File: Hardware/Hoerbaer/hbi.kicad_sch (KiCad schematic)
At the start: 50 parts, among them J10 LEDS, J11 LEDS, J6 BUTTONS, J7 BUTTONS, J8 BUTTONS, J9 LEDS, U2 PCF8574TS, U3 PCF8574TS, U4 PCF8574TS, U5 TLC59108xPW, U6 TLC59108xPW, U7 TLC59108xPW

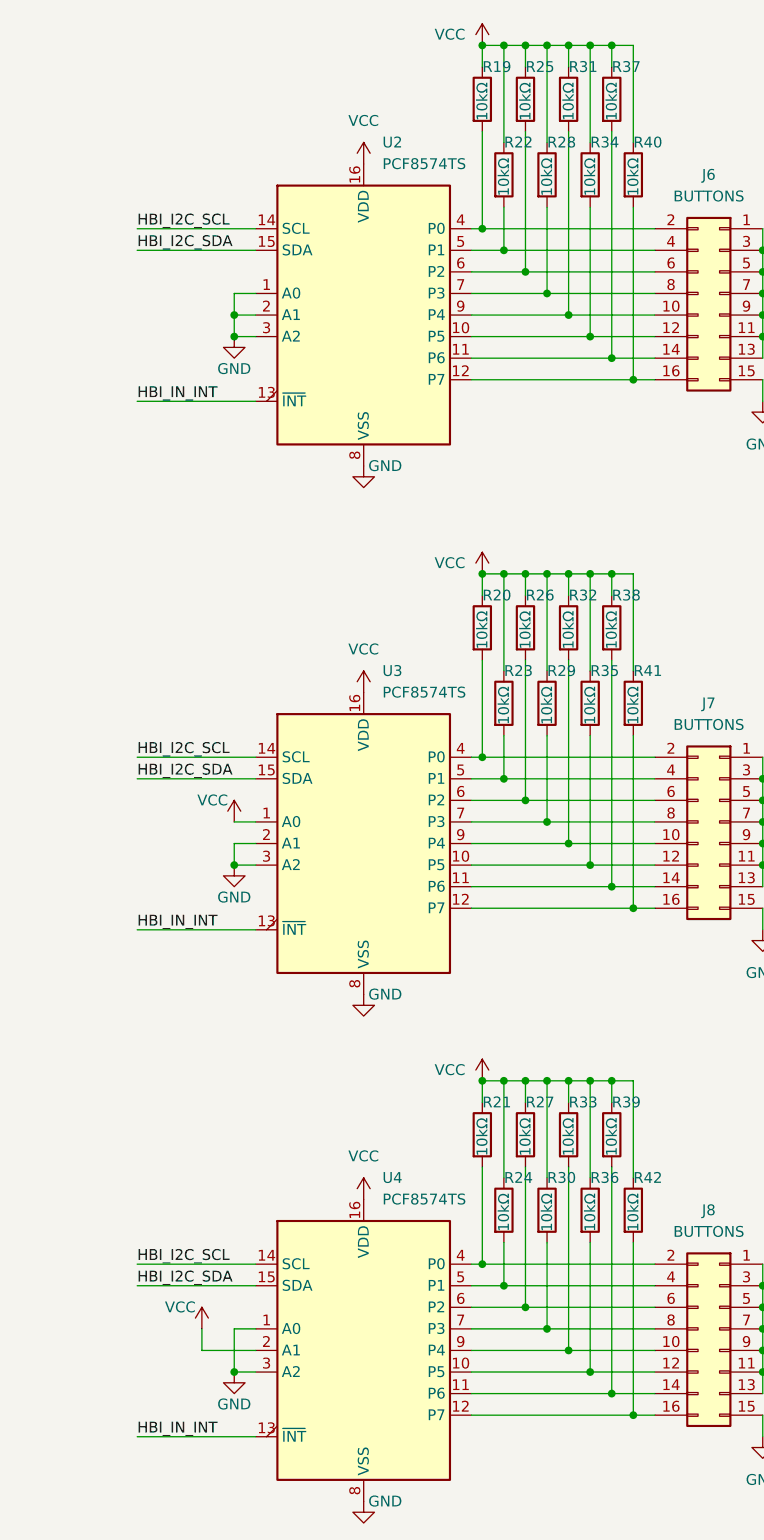
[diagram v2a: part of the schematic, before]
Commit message: More numbers, changed HBI input package, i2c addresses, layout.
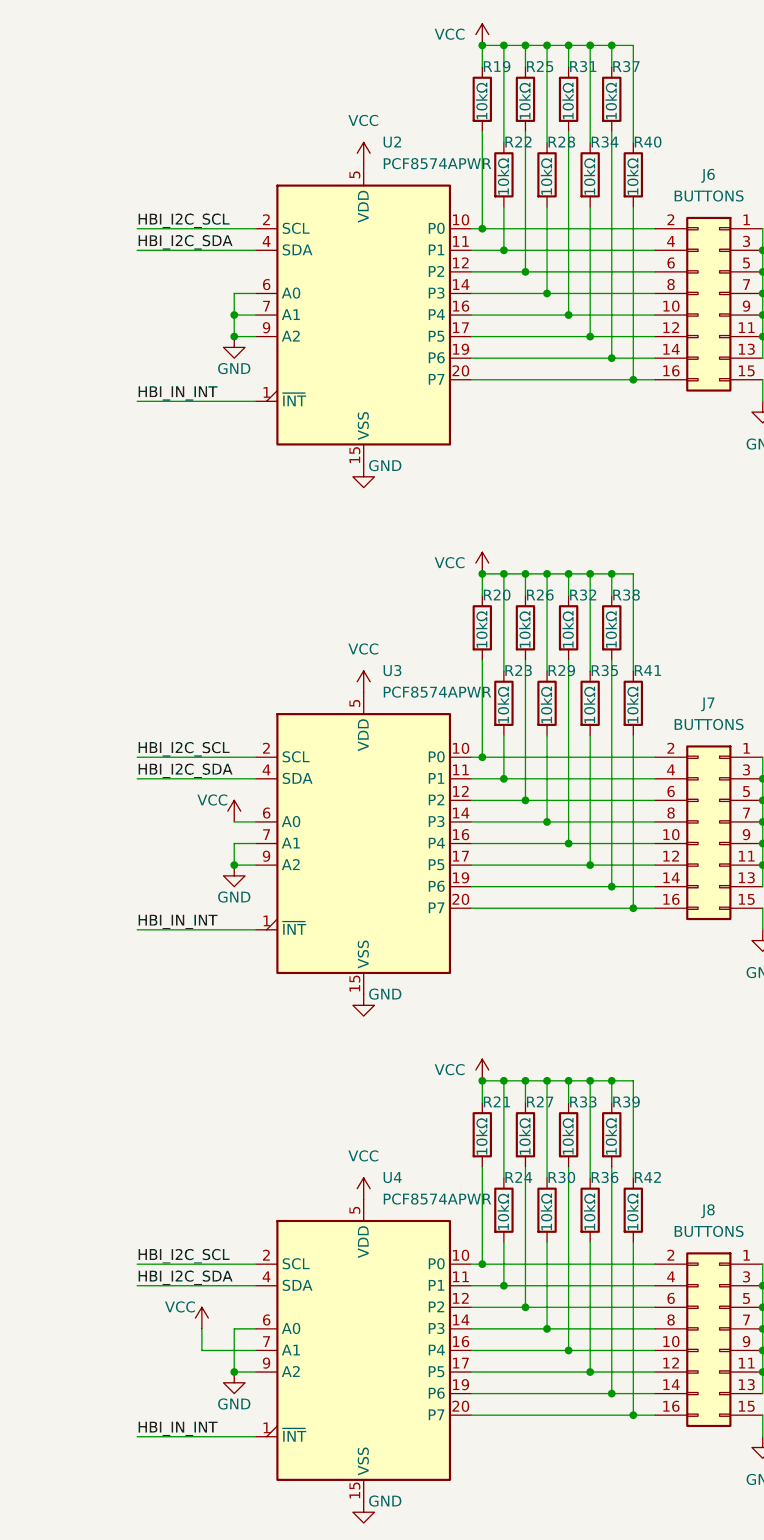
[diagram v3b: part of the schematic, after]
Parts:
- U2, U3, U4: value PCF8574TS -> PCF8574APWR; footprint Package_SO:SOIC-16W_7.5x10.3mm_P1.27mm -> Package_SO:SSOP-20_4.4x6.5mm_P0.65mm; symbol Interface_Expansion:PCF8574A -> Interface_Expansion:PCF8574ATS; JLCPCB C2987289 -> C94361; MPN PCF8574AT/TR -> PCF8574APWR
- U5: JLCPCB (none) -> C130031; MPN (none) -> TLC59108IPWR
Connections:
- net GND: now also U2.15 (VSS), U2.6 (A0), U2.7 (A1), U2.9 (A2), U3.15 (VSS), U3.7 (A1), U3.9 (A2), U4.15 (VSS), U4.6 (A0), U4.9 (A2); no longer U2.1 (A0), U2.2 (A1), U2.3 (A2), U2.8 (VSS), U3.2 (A1), U3.3 (A2), U3.8 (VSS), U4.1 (A0), U4.3 (A2), U4.8 (VSS)
- net HBI_I2C_SCL: now also U2.2 (SCL), U3.2 (SCL), U4.2 (SCL); no longer U2.14 (SCL), U3.14 (SCL), U4.14 (SCL)
- net HBI_I2C_SDA: now also U2.4 (SDA), U3.4 (SDA), U4.4 (SDA); no longer U2.15 (SDA), U3.15 (SDA), U4.15 (SDA)
- net HBI_IN_INT: now also U2.1 (~{INT}), U3.1 (~{INT}), U4.1 (~{INT}); no longer U2.13 (~{INT}), U3.13 (~{INT}), U4.13 (~{INT})
- net VCC: now also U2.5 (VDD), U3.5 (VDD), U3.6 (A0), U4.5 (VDD), U4.7 (A1); no longer U2.16 (VDD), U3.1 (A0), U3.16 (VDD), U4.16 (VDD), U4.2 (A1)
- net at J8.4 (Pin_4), R24.2: now also U4.11 (P1); no longer U4.5 (P1)
- net at J6.2 (Pin_2), R19.2: now also U2.10 (P0); no longer U2.4 (P0)
- net at J7.8 (Pin_8), R29.2: now also U3.14 (P3); no longer U3.7 (P3)
- net at J8.12 (Pin_12), R36.2: now also U4.17 (P5); no longer U4.10 (P5)
- net at J8.14 (Pin_14), R39.2: now also U4.19 (P6); no longer U4.11 (P6)
- net at J8.16 (Pin_16), R42.2: now also U4.20 (P7); no longer U4.12 (P7)
- net at J8.2 (Pin_2), R21.2: now also U4.10 (P0); no longer U4.4 (P0)
- net at J8.6 (Pin_6), R27.2: now also U4.12 (P2); no longer U4.6 (P2)
- net at J8.8 (Pin_8), R30.2: now also U4.14 (P3); no longer U4.7 (P3)
- net at J8.10 (Pin_10), R33.2: now also U4.16 (P4); no longer U4.9 (P4)
- net at J7.12 (Pin_12), R35.2: now also U3.17 (P5); no longer U3.10 (P5)
- net at J7.14 (Pin_14), R38.2: now also U3.19 (P6); no longer U3.11 (P6)
- net at J7.16 (Pin_16), R41.2: now also U3.20 (P7); no longer U3.12 (P7)
- net at J7.2 (Pin_2), R20.2: now also U3.10 (P0); no longer U3.4 (P0)
- net at J7.4 (Pin_4), R23.2: now also U3.11 (P1); no longer U3.5 (P1)
- net at J7.6 (Pin_6), R26.2: now also U3.12 (P2); no longer U3.6 (P2)
- net at J7.10 (Pin_10), R32.2: now also U3.16 (P4); no longer U3.9 (P4)
- net at J6.6 (Pin_6), R25.2: now also U2.12 (P2); no longer U2.6 (P2)
- net at J6.12 (Pin_12), R34.2: now also U2.17 (P5); no longer U2.10 (P5)
- net at J6.10 (Pin_10), R31.2: now also U2.16 (P4); no longer U2.9 (P4)
- net at J6.14 (Pin_14), R37.2: now also U2.19 (P6); no longer U2.11 (P6)
- net at J6.16 (Pin_16), R40.2: now also U2.20 (P7); no longer U2.12 (P7)
- net at J6.4 (Pin_4), R22.2: now also U2.11 (P1); no longer U2.5 (P1)
- net at J6.8 (Pin_8), R28.2: now also U2.14 (P3); no longer U2.7 (P3)

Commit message: Layout drc error free
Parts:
- removed J10, J11, J9: LEDS, Connector_PinHeader_2.54mm:PinHeader_2x08_P2.54mm_Vertical, symbol Connector_Generic:Conn_02x08_Odd_Even
- removed J7, J8: BUTTONS, Connector_PinHeader_2.54mm:PinHeader_2x08_P2.54mm_Vertical, symbol Connector_Generic:Conn_02x08_Odd_Even
- added C65: 10µF, Capacitor_SMD:C_0805_2012Metric, symbol Device:C
- added J7: PAW_B, Connector_PinHeader_2.54mm:PinHeader_2x12_P2.54mm_Vertical, symbol Connector_Generic:Conn_02x12_Odd_Even
- added J8: PAW_C, Connector_PinHeader_2.54mm:PinHeader_2x12_P2.54mm_Vertical, symbol Connector_Generic:Conn_02x12_Odd_Even
- added J9: PAW_D, Connector_PinHeader_2.54mm:PinHeader_2x12_P2.54mm_Vertical, symbol Connector_Generic:Conn_02x12_Odd_Even
- J6: value BUTTONS -> PAW_A; footprint Connector_PinHeader_2.54mm:PinHeader_2x08_P2.54mm_Vertical -> Connector_PinHeader_2.54mm:PinHeader_2x12_P2.54mm_Vertical; symbol Connector_Generic:Conn_02x08_Odd_Even -> Connector_Generic:Conn_02x12_Odd_Even
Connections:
- net +12V: now also J6.12 (Pin_12), J6.16 (Pin_16), J6.20 (Pin_20), J6.24 (Pin_24), J6.4 (Pin_4), J6.8 (Pin_8), C65.1, J7.12 (Pin_12), J7.16 (Pin_16), J7.20 (Pin_20), J7.24 (Pin_24), J7.4 (Pin_4), J7.8 (Pin_8), J8.12 (Pin_12), J8.16 (Pin_16), J8.20 (Pin_20), J8.24 (Pin_24), J8.4 (Pin_4), J8.8 (Pin_8), J9.12 (Pin_12), J9.16 (Pin_16), J9.20 (Pin_20), J9.24 (Pin_24), J9.4 (Pin_4), J9.8 (Pin_8)
- net GND: now also J6.10 (Pin_10), J6.14 (Pin_14), J6.18 (Pin_18), J6.2 (Pin_2), J6.22 (Pin_22), J6.6 (Pin_6), C65.2, J7.10 (Pin_10), J7.14 (Pin_14), J7.18 (Pin_18), J7.2 (Pin_2), J7.22 (Pin_22), J7.6 (Pin_6), J8.10 (Pin_10), J8.14 (Pin_14), J8.18 (Pin_18), J8.2 (Pin_2), J8.22 (Pin_22), J8.6 (Pin_6), J9.10 (Pin_10), J9.14 (Pin_14), J9.18 (Pin_18), J9.2 (Pin_2), J9.22 (Pin_22), J9.6 (Pin_6); no longer J6.15 (Pin_15)
- net PAW_C_B6: now reaches R24.2, U4.11 (P1)
- net PAW_C_B6: now also J8.21 (Pin_21)
- net PAW_A_B1: now reaches R19.2, U2.10 (P0)
- net PAW_A_B1: now also J6.1 (Pin_1); no longer J6.2 (Pin_2)
- net PAW_B_B6: now reaches R29.2, U3.14 (P3)
- net PAW_B_B6: now also J7.21 (Pin_21)
- net PAW_C_B5: now reaches R21.2, U4.10 (P0)
- net PAW_C_B5: now also J8.17 (Pin_17)
- net PAW_D_B1: now reaches R27.2, U4.12 (P2)
- net PAW_D_B1: now also J9.1 (Pin_1)
- net PAW_D_B2: now reaches R30.2, U4.14 (P3)
- net PAW_D_B2: now also J9.5 (Pin_5)
- net PAW_D_B3: now reaches R33.2, U4.16 (P4)
- net PAW_D_B3: now also J9.9 (Pin_9)
- net PAW_D_B4: now reaches R36.2, U4.17 (P5)
- net PAW_D_B4: now also J9.13 (Pin_13)
- net PAW_D_B5: now reaches R39.2, U4.19 (P6)
- net PAW_D_B5: now also J9.17 (Pin_17)
- net PAW_D_B6: now reaches R42.2, U4.20 (P7)
- net PAW_D_B6: now also J9.21 (Pin_21)
- net PAW_B_B3: now reaches R20.2, U3.10 (P0)
- net PAW_B_B3: now also J7.9 (Pin_9)
- net PAW_B_B4: now reaches R23.2, U3.11 (P1)
- net PAW_B_B4: now also J7.13 (Pin_13)
- net PAW_B_B5: now reaches R26.2, U3.12 (P2)
- net PAW_B_B5: now also J7.17 (Pin_17)
- net PAW_C_B1: now reaches R32.2, U3.16 (P4)
- net PAW_C_B1: now also J8.1 (Pin_1)
- net PAW_C_B2: now reaches R35.2, U3.17 (P5)
- net PAW_C_B2: now also J8.5 (Pin_5)
- net PAW_C_B3: now reaches R38.2, U3.19 (P6)
- net PAW_C_B3: now also J8.9 (Pin_9)
- net PAW_C_B4: now reaches R41.2, U3.20 (P7)
- net PAW_C_B4: now also J8.13 (Pin_13)
- net PAW_A_B3: now reaches R25.2, U2.12 (P2)
- net PAW_A_B3: now also J6.9 (Pin_9); no longer J6.6 (Pin_6)
- net PAW_D_D2: now reaches U7.10 (~{OUT3})
- net PAW_D_D2: now also J9.7 (Pin_7)
- net PAW_D_D3: now reaches U7.11 (~{OUT4})
- net PAW_D_D3: now also J9.11 (Pin_11)
- net PAW_D_D4: now reaches U7.12 (~{OUT5})
- net PAW_D_D4: now also J9.15 (Pin_15)
- net PAW_D_D5: now reaches U7.14 (~{OUT6})
- net PAW_D_D5: now also J9.19 (Pin_19)
- net PAW_D_D6: now reaches U7.15 (~{OUT7})
- net PAW_D_D6: now also J9.23 (Pin_23)
- net PAW_C_D5: now reaches U7.6 (~{OUT0})
- net PAW_C_D5: now also J8.19 (Pin_19)
- net PAW_C_D6: now reaches U7.7 (~{OUT1})
- net PAW_C_D6: now also J8.23 (Pin_23)
- net PAW_D_D1: now reaches U7.9 (~{OUT2})
- net PAW_D_D1: now also J9.3 (Pin_3)
- net PAW_A_B6: now reaches R34.2, U2.17 (P5)
- net PAW_A_B6: now also J6.21 (Pin_21); no longer J6.12 (Pin_12)
- net PAW_A_B5: now reaches R31.2, U2.16 (P4)
- net PAW_A_B5: now also J6.17 (Pin_17); no longer J6.10 (Pin_10)
- net PAW_B_B1: now reaches R37.2, U2.19 (P6)
- net PAW_B_B1: now also J7.1 (Pin_1); no longer J6.14 (Pin_14)
- net PAW_B_B2: now reaches R40.2, U2.20 (P7)
- net PAW_B_B2: now also J7.5 (Pin_5); no longer J6.16 (Pin_16)
- net PAW_A_B2: now reaches R22.2, U2.11 (P1)
- net PAW_A_B2: now also J6.5 (Pin_5); no longer J6.4 (Pin_4)
- net PAW_A_B4: now reaches R28.2, U2.14 (P3)
- net PAW_A_B4: now also J6.13 (Pin_13); no longer J6.8 (Pin_8)
- net PAW_A_D4: now reaches U5.10 (~{OUT3})
- net PAW_A_D4: now also J6.15 (Pin_15)
- net PAW_A_D5: now reaches U5.11 (~{OUT4})
- net PAW_A_D5: now also J6.19 (Pin_19)
- net PAW_A_D6: now reaches U5.12 (~{OUT5})
- net PAW_A_D6: now also J6.23 (Pin_23)
- net PAW_B_D1: now reaches U5.14 (~{OUT6})
- net PAW_B_D1: now also J7.3 (Pin_3)
- net PAW_B_D2: now reaches U5.15 (~{OUT7})
- net PAW_B_D2: now also J7.7 (Pin_7)
- net PAW_A_D1: now reaches U5.6 (~{OUT0})
- net PAW_A_D1: now also J6.3 (Pin_3)
- net PAW_A_D2: now reaches U5.7 (~{OUT1})
- net PAW_A_D2: now also J6.7 (Pin_7)
- net PAW_A_D3: now reaches U5.9 (~{OUT2})
- net PAW_A_D3: now also J6.11 (Pin_11)
- net PAW_B_D6: now reaches U6.10 (~{OUT3})
- net PAW_B_D6: now also J7.23 (Pin_23)
- net PAW_C_D1: now reaches U6.11 (~{OUT4})
- net PAW_C_D1: now also J8.3 (Pin_3)
- net PAW_C_D2: now reaches U6.12 (~{OUT5})
- net PAW_C_D2: now also J8.7 (Pin_7)
- net PAW_C_D3: now reaches U6.14 (~{OUT6})
- net PAW_C_D3: now also J8.11 (Pin_11)
- net PAW_C_D4: now reaches U6.15 (~{OUT7})
- net PAW_C_D4: now also J8.15 (Pin_15)
- net PAW_B_D3: now reaches U6.6 (~{OUT0})
- net PAW_B_D3: now also J7.11 (Pin_11)
- net PAW_B_D4: now reaches U6.7 (~{OUT1})
- net PAW_B_D4: now also J7.15 (Pin_15)
- net PAW_B_D5: now reaches U6.9 (~{OUT2})
- net PAW_B_D5: now also J7.19 (Pin_19)
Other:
- note removed: "R_{EXT} 2kΩ => LED current: 1mA"
- moved on the sheet: C10, C11, C22, C23, C24, C6, C7, C8, C9, R19, R20, R21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

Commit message: Order numbers
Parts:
- C10, C11, C6, C7, C8, C9: JLCPCB (none) -> C458949; MPN (none) -> MT15B104K160CT
- U6, U7: JLCPCB (none) -> C130031; MPN (none) -> TLC59108IPWR
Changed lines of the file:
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@@
+      (effects (font (size 1.27 1.27)) hide)
+    )
+    (property "JLCPCB" "C458949" (at 99.06 110.49 0)
+      (effects (font (size 1.27 1.27)) hide)
+    )
+    (property "MPN" "MT15B104K160CT" (at 99.06 110.49 0)
       (effects (font (size 1.27 1.27)) hide)
     )
@@
       (effects (font (size 1.27 1.27)) hide)
     )
+    (property "JLCPCB" "C130031" (at 242.57 139.7 0)
+      (effects (font (size 1.27 1.27)) hide)
+    )
+    (property "MPN" "TLC59108IPWR" (at 242.57 139.7 0)
+      (effects (font (size 1.27 1.27)) hide)
+    )
     (pin "1")
     (pin "10")
@@
       (effects (font (size 1.27 1.27)) hide)
     )
+    (property "JLCPCB" "C458949" (at 214.63 46.99 0)
+      (effects (font (size 1.27 1.27)) hide)
+    )
+    (property "MPN" "MT15B104K160CT" (at 214.63 46.99 0)
+      (effects (font (size 1.27 1.27)) hide)
+    )
     (pin "1")
     (pin "2")
@@
       (effects (font (size 1.27 1.27)) hide)
     )
+    (property "JLCPCB" "C458949" (at 99.06 48.26 0)
+      (effects (font (size 1.27 1.27)) hide)
+    )
+    (property "MPN" "MT15B104K160CT" (at 99.06 48.26 0)
+      (effects (font (size 1.27 1.27)) hide)
+    )
     (pin "1")
     (pin "2")
@@
       (effects (font (size 1.27 1.27)) hide)
     )
+    (property "JLCPCB" "C458949" (at 214.63 151.13 0)
+      (effects (font (size 1.27 1.27)) hide)
+    )
+    (property "MPN" "MT15B104K160CT" (at 214.63 151.13 0)
+      (effects (font (size 1.27 1.27)) hide)
+    )
     (pin "1")
     (pin "2")
@@
     )
     (property "Datasheet" "~" (at 99.06 170.18 0)
+      (effects (font (size 1.27 1.27)) hide)
+    )
+    (property "JLCPCB" "C458949" (at 99.06 170.18 0)
+      (effects (font (size 1.27 1.27)) hide)
+    )
+    (property "MPN" "MT15B104K160CT" (at 99.06 170.18 0)
       (effects (font (size 1.27 1.27)) hide)
     )
@@
       (effects (font (size 1.27 1.27)) hide)
     )
+    (property "JLCPCB" "C130031" (at 242.57 90.17 0)
+      (effects (font (size 1.27 1.27)) hide)
+    )
+    (property "MPN" "TLC59108IPWR" (at 242.57 90.17 0)
+      (effects (font (size 1.27 1.27)) hide)
+    )
     (pin "1")
     (pin "10")
@@
       (effects (font (size 1.27 1.27)) hide)
     )
+    (property "JLCPCB" "C458949" (at 214.63 101.6 0)
+      (effects (font (size 1.27 1.27)) hide)
+    )
+    (property "MPN" "MT15B104K160CT" (at 214.63 101.6 0)
+      (effects (font (size 1.27 1.27)) hide)
+    )

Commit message: Renamed JLCPCB attribute to LCSC (plugin search list)
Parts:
- C10, C11, C6, C7, C8, C9: JLCPCB C458949 -> (none); LCSC (none) -> C458949
- C22, C23, C24, C65: JLCPCB C6119932 -> (none); LCSC (none) -> C6119932
- U2, U3, U4: JLCPCB C94361 -> (none); LCSC (none) -> C94361
- U5, U6, U7: JLCPCB C130031 -> (none); LCSC (none) -> C130031
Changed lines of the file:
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@@
       (effects (font (size 1.27 1.27)) hide)
     )
-    (property "JLCPCB" "C458949" (at 99.06 110.49 0)
+    (property "LCSC" "C458949" (at 99.06 110.49 0)
       (effects (font (size 1.27 1.27)) hide)
     )
@@
       (effects (font (size 1.27 1.27)) hide)
     )
-    (property "JLCPCB" "C94361" (at 130.81 172.72 0)
+    (property "LCSC" "C94361" (at 130.81 172.72 0)
       (effects (font (size 1.27 1.27)) hide)
     )
@@
       (effects (font (size 1.27 1.27)) hide)
     )
-    (property "JLCPCB" "C94361" (at 130.81 113.03 0)
+    (property "LCSC" "C94361" (at 130.81 113.03 0)
       (effects (font (size 1.27 1.27)) hide)
     )
@@
       (effects (font (size 1.27 1.27)) hide)
     )
-    (property "JLCPCB" "C130031" (at 242.57 139.7 0)
+    (property "LCSC" "C130031" (at 242.57 139.7 0)
       (effects (font (size 1.27 1.27)) hide)
     )
@@
       (effects (font (size 1.27 1.27)) hide)
     )
-    (property "JLCPCB" "C6119932" (at 64.77 64.77 0)
+    (property "LCSC" "C6119932" (at 64.77 64.77 0)
       (effects (font (size 1.27 1.27)) hide)
     )
@@
       (effects (font (size 1.27 1.27)) hide)
     )
-    (property "JLCPCB" "C130031" (at 242.57 39.37 0)
+    (property "LCSC" "C130031" (at 242.57 39.37 0)
       (effects (font (size 1.27 1.27)) hide)
     )
@@
       (effects (font (size 1.27 1.27)) hide)
     )
-    (property "JLCPCB" "C458949" (at 214.63 46.99 0)
+    (property "LCSC" "C458949" (at 214.63 46.99 0)
       (effects (font (size 1.27 1.27)) hide)
     )
@@
       (effects (font (size 1.27 1.27)) hide)
     )
-    (property "JLCPCB" "C6119932" (at 77.47 64.77 0)
+    (property "LCSC" "C6119932" (at 77.47 64.77 0)
       (effects (font (size 1.27 1.27)) hide)
     )
@@
       (effects (font (size 1.27 1.27)) hide)
     )
-    (property "JLCPCB" "C458949" (at 99.06 48.26 0)
+    (property "LCSC" "C458949" (at 99.06 48.26 0)
       (effects (font (size 1.27 1.27)) hide)
     )
@@
       (effects (font (size 1.27 1.27)) hide)
     )
-    (property "JLCPCB" "C458949" (at 214.63 151.13 0)
+    (property "LCSC" "C458949" (at 214.63 151.13 0)
       (effects (font (size 1.27 1.27)) hide)
     )
@@
       (effects (font (size 1.27 1.27)) hide)
     )
-    (property "JLCPCB" "C458949" (at 99.06 170.18 0)
+    (property "LCSC" "C458949" (at 99.06 170.18 0)
       (effects (font (size 1.27 1.27)) hide)
     )
@@
       (effects (font (size 1.27 1.27)) hide)
     )
-    (property "JLCPCB" "C130031" (at 242.57 90.17 0)
+    (property "LCSC" "C130031" (at 242.57 90.17 0)
       (effects (font (size 1.27 1.27)) hide)
     )
@@
       (effects (font (size 1.27 1.27)) hide)
     )
-    (property "JLCPCB" "C94361" (at 130.81 50.8 0)
+    (property "LCSC" "C94361" (at 130.81 50.8 0)
       (effects (font (size 1.27 1.27)) hide)
     )
@@
       (effects (font (size 1.27 1.27)) hide)
     )
-    (property "JLCPCB" "C6119932" (at 64.77 45.72 0)
+    (property "LCSC" "C6119932" (at 64.77 45.72 0)
       (effects (font (size 1.27 1.27)) hide)
     )
@@
       (effects (font (size 1.27 1.27)) hide)
     )
-    (property "JLCPCB" "C458949" (at 214.63 101.6 0)
+    (property "LCSC" "C458949" (at 214.63 101.6 0)
       (effects (font (size 1.27 1.27)) hide)
     )
@@
       (effects (font (size 1.27 1.27)) hide)
     )
-    (property "JLCPCB" "C6119932" (at 77.47 45.72 0)
-      (effects (font (size 1.27 1.27)) hide)
-    )
+    (property "LCSC" "C6119932" (at 77.47 45.72 0)
+      (effects (font (size 1.27 1.27)) hide)
+    )
